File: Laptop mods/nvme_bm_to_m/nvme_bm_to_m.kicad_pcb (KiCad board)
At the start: 2 copper layers, 22 x 12.4 mm, 9 parts, among them J1 USB, U1 NGFF_M, U2 NGFF_B

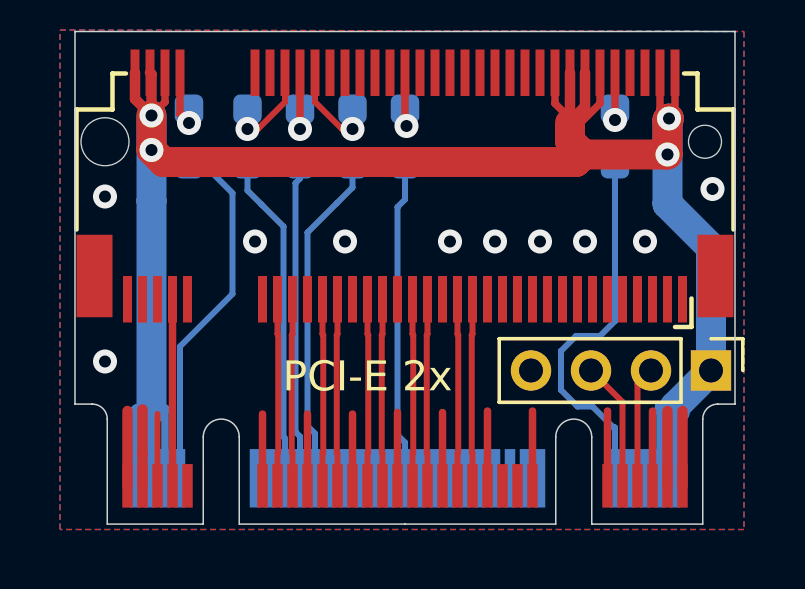
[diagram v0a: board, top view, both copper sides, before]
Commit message: Adding GND to the NVMe BM to M card shield
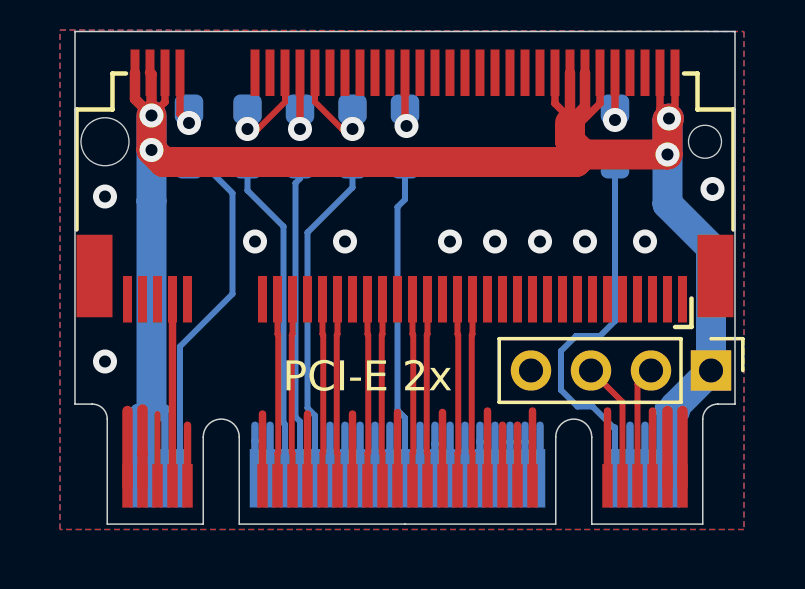
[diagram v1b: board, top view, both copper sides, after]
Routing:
- net Net-(U2-Pad67): track 0.00 -> 2.02 mm
- net Net-(U2-Pad25): track 0.00 -> 2.02 mm
- net Net-(U2-Pad23): track 0.00 -> 2.02 mm
- net Net-(U2-Pad8): track 0.00 -> 1.77 mm
- net Net-(U2-Pad6): track 0.00 -> 1.77 mm
- net Net-(U2-Pad58): track 0.00 -> 1.77 mm
- net Net-(U2-Pad56): track 0.00 -> 1.77 mm
- net Net-(U2-Pad48): track 0.00 -> 1.77 mm
- net Net-(U2-Pad46): track 0.00 -> 1.77 mm
- net Net-(U2-Pad44): track 0.00 -> 1.77 mm
- net Net-(U2-Pad42): track 0.00 -> 1.77 mm
- net Net-(U2-Pad40): track 0.00 -> 1.77 mm
- net Net-(U2-Pad36): track 0.00 -> 1.77 mm
- net Net-(U2-Pad34): track 0.00 -> 1.77 mm
- net Net-(U2-Pad32): track 0.00 -> 1.77 mm
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
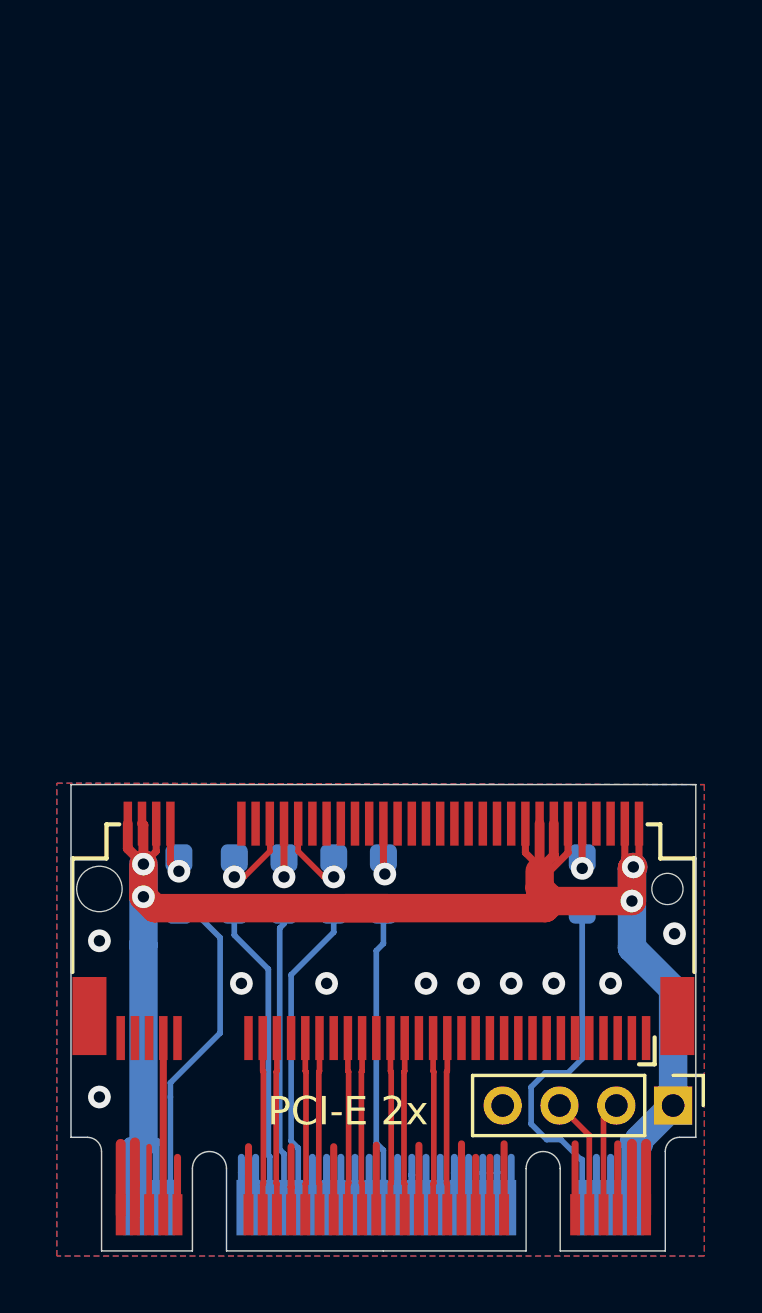
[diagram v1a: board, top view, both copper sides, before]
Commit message: Rerouted diffpairs to NVMe BM to M adapter, made the adapter longer, added holes so that part of the adapter can be snipped off for length decrease
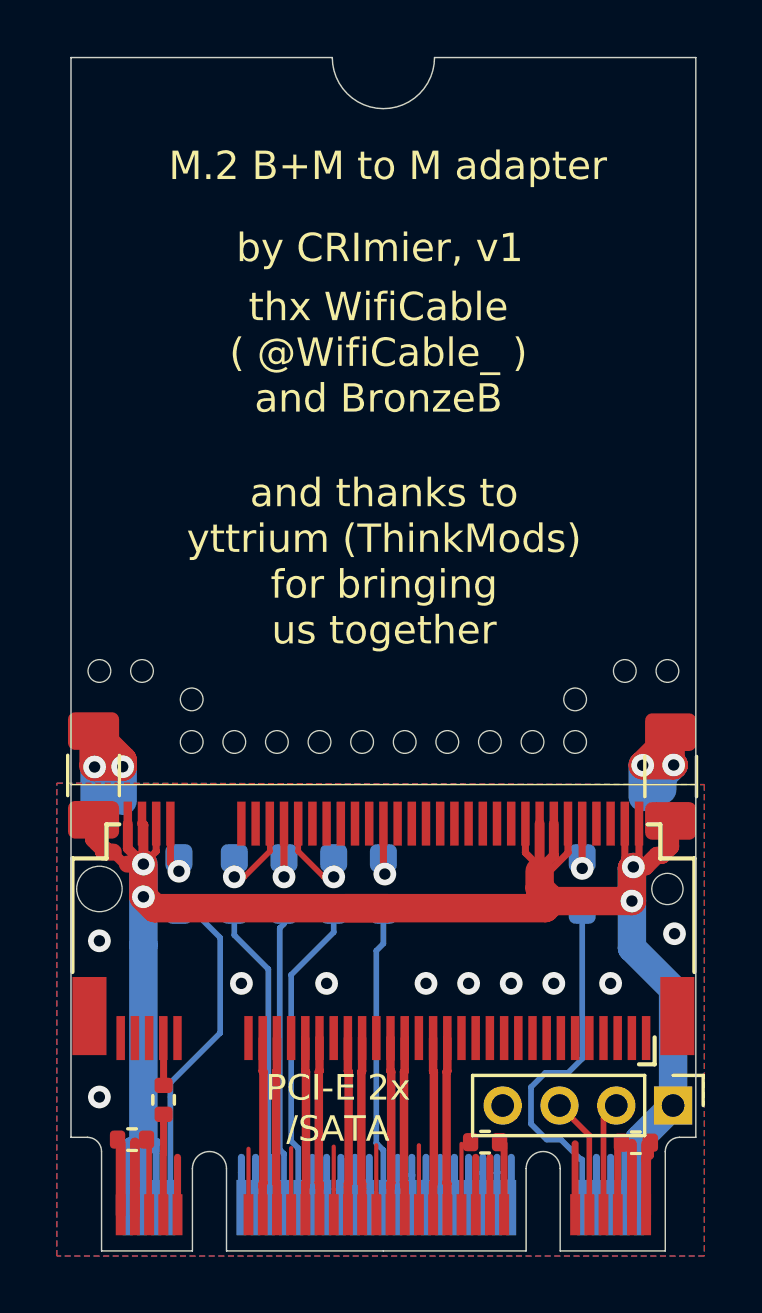
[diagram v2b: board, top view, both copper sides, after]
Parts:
- added C1: C_Small, Capacitor_SMD:C_1206_3216Metric_Pad1.33x1.80mm_HandSolder, F.Cu at (129.8, 154.2)
- added C2: C_Small, Capacitor_SMD:C_1206_3216Metric_Pad1.33x1.80mm_HandSolder, F.Cu at (150.1, 154.2)
- added R10: 0R, Resistor_SMD:R_0402_1005Metric, F.Cu at (131.2, 167.0)
- added R7: 0R, Resistor_SMD:R_0402_1005Metric, F.Cu at (148.9, 167.1)
- added R8: 0R, Resistor_SMD:R_0402_1005Metric, F.Cu at (143.6, 167.1)
- added R9: 0R, Resistor_SMD:R_0402_1005Metric, F.Cu at (132.3, 165.6)
- added REF**: hole, nvme_bm_to_m:hole, F.Cu at (146.8, 151.5)
- added REF**: hole, nvme_bm_to_m:hole, F.Cu at (137.8, 153.0)
- added REF**: hole, nvme_bm_to_m:hole, F.Cu at (136.2, 153.0)
- added REF**: hole, nvme_bm_to_m:hole, F.Cu at (134.8, 153.0)
- added REF**: hole, nvme_bm_to_m:hole, F.Cu at (130.0, 150.5)
- added REF**: hole, nvme_bm_to_m:hole, F.Cu at (131.5, 150.5)
- added REF**: hole, nvme_bm_to_m:hole, F.Cu at (133.2, 151.5)
- added REF**: hole, nvme_bm_to_m:hole, F.Cu at (133.2, 153.0)
- added REF**: hole, nvme_bm_to_m:hole, F.Cu at (148.5, 150.5)
- added REF**: hole, nvme_bm_to_m:hole, F.Cu at (150.0, 150.5)
- added REF**: hole, nvme_bm_to_m:hole, F.Cu at (146.8, 153.0)
- added REF**: hole, nvme_bm_to_m:hole, F.Cu at (145.2, 153.0)
- added REF**: hole, nvme_bm_to_m:hole, F.Cu at (143.8, 153.0)
- added REF**: hole, nvme_bm_to_m:hole, F.Cu at (142.2, 153.0)
- added REF**: hole, nvme_bm_to_m:hole, F.Cu at (140.8, 153.0)
- added REF**: hole, nvme_bm_to_m:hole, F.Cu at (139.2, 153.0)
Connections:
- U2 pad 1: GND -> Net-(R7-Pad1)
- U2 pad 21: GND -> Net-(R8-Pad1)
- U2 pad 69: /PCIE_~SATA -> Net-(R9-Pad1)
- U2 pad 75: GND -> Net-(R10-Pad1)
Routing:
- net +3V3: track 73.2 -> 82.0 mm
- net GND: track 34.5 -> 41.6 mm, vias 10 -> 14
- net /PCIE_~SATA: track 6.22 -> 1.67 mm
- net Net-(R9-Pad1): track 0.00 -> 3.54 mm
- net Net-(R7-Pad1): track 0.00 -> 3.16 mm
- net Net-(R8-Pad1): track 0.00 -> 2.50 mm
- net Net-(R10-Pad1): track 0.00 -> 2.50 mm
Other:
- board size 22 x 12.4 mm -> 22 x 38 mm
- rule trace_min: 0.2 -> 0.15
- board text added: "PCI-E 2x /SATA"
- board text added: "and thanks to yttrium (ThinkMods) for bringing us together"
- board text added: "thx WifiCable ( @WifiCable_ ) and BronzeB"
- board text removed: "PCI-E 2x"

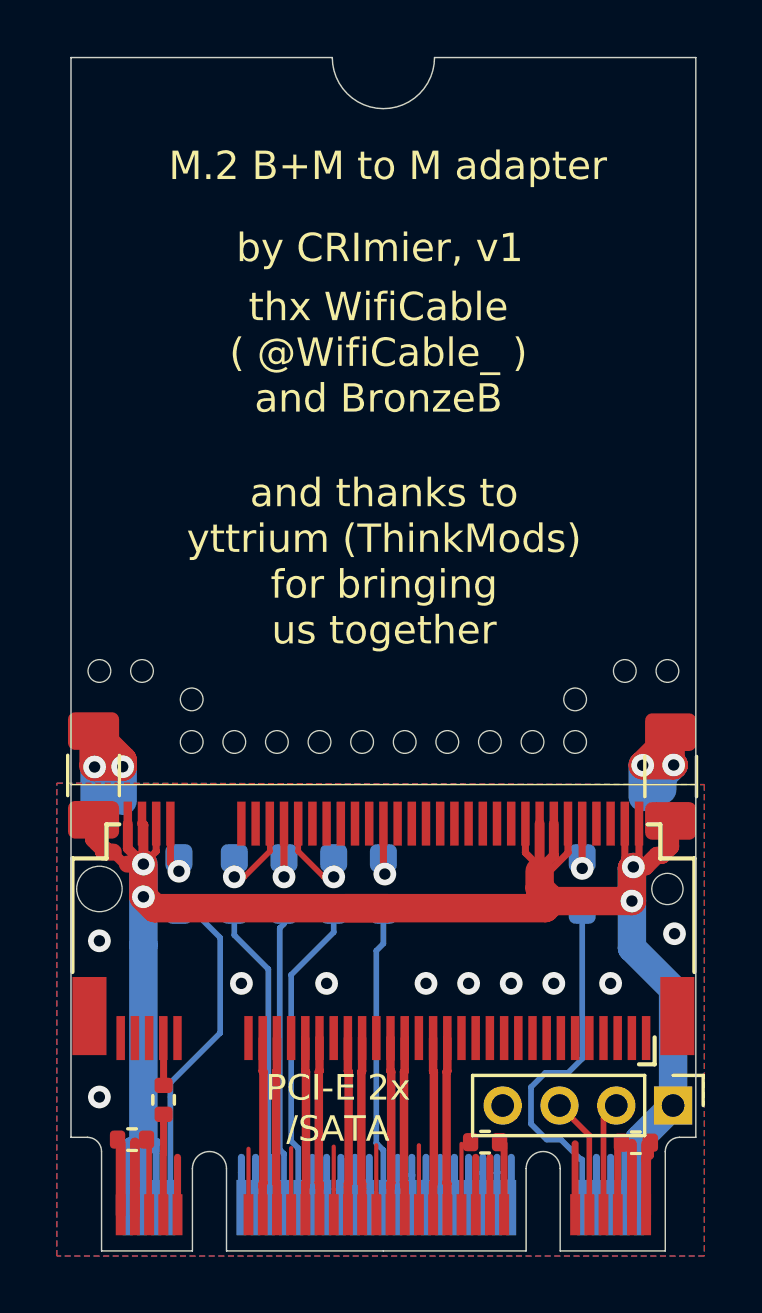
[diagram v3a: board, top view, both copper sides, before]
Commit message: nvme_bm_to_m: v2, removed caps, changed shape, isolated one ambiguous pin, updated README
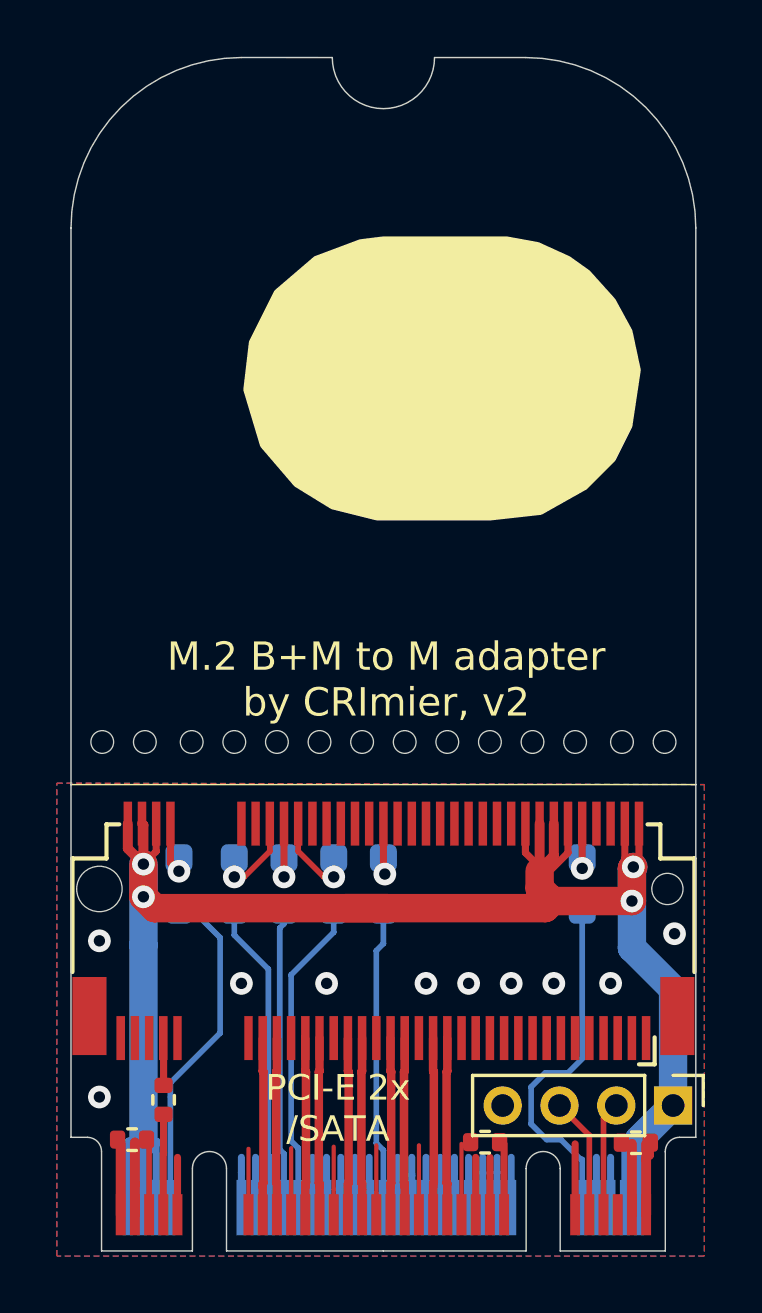
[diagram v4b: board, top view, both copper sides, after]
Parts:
- removed C1, C2: C_Small, Capacitor_SMD:C_1206_3216Metric_Pad1.33x1.80mm_HandSolder
- removed the REF** at (146.8, 151.5)
- removed the REF** at (133.2, 151.5)
- moved REF** 2.50 mm to (149.9, 153.0)
- moved REF** 2.50 mm to (148.4, 153.0)
- moved REF** 2.50 mm to (131.6, 153.0)
- moved REF** 2.50 mm to (130.1, 153.0)
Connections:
- net /PCIE_~SATA renamed /PCIE_~{SATA}
- net ~CLKREQ renamed ~{CLKREQ}
- net ~PERST renamed ~{PERST}
- net ~PEWAKE renamed ~{PEWAKE}
- U1 pad 11: Net-(U1-Pad11) -> unconnected-(U1-Pad11)
- U1 pad 13: Net-(U1-Pad13) -> unconnected-(U1-Pad13)
- U1 pad 17: Net-(U1-Pad17) -> unconnected-(U1-Pad17)
- U1 pad 19: Net-(U1-Pad19) -> unconnected-(U1-Pad19)
- U1 pad 20: Net-(U1-Pad20) -> unconnected-(U1-Pad20)
- U1 pad 22: Net-(U1-Pad22) -> unconnected-(U1-Pad22)
- U1 pad 23: Net-(U1-Pad23) -> unconnected-(U1-Pad23)
- U1 pad 24: Net-(U1-Pad24) -> unconnected-(U1-Pad24)
- U1 pad 25: Net-(U1-Pad25) -> unconnected-(U1-Pad25)
- U1 pad 26: Net-(U1-Pad26) -> unconnected-(U1-Pad26)
- U1 pad 28: Net-(U1-Pad28) -> unconnected-(U1-Pad28)
- U1 pad 30: Net-(U1-Pad30) -> unconnected-(U1-Pad30)
- U1 pad 32: Net-(U1-Pad32) -> unconnected-(U1-Pad32)
- U1 pad 34: Net-(U1-Pad34) -> unconnected-(U1-Pad34)
- U1 pad 36: Net-(U1-Pad36) -> unconnected-(U1-Pad36)
- U1 pad 40: Net-(U1-Pad40) -> unconnected-(U1-Pad40)
- U1 pad 42: Net-(U1-Pad42) -> unconnected-(U1-Pad42)
- U1 pad 44: Net-(U1-Pad44) -> unconnected-(U1-Pad44)
- U1 pad 46: Net-(U1-Pad46) -> unconnected-(U1-Pad46)
- U1 pad 48: Net-(U1-Pad48) -> unconnected-(U1-Pad48)
- U1 pad 5: Net-(U1-Pad5) -> unconnected-(U1-Pad5)
- U1 pad 56: Net-(U1-Pad56) -> unconnected-(U1-Pad56)
- U1 pad 58: Net-(U1-Pad58) -> unconnected-(U1-Pad58)
- U1 pad 6: Net-(U1-Pad6) -> unconnected-(U1-Pad6)
- U1 pad 67: Net-(U1-Pad67) -> unconnected-(U1-Pad67)
- U1 pad 7: Net-(U1-Pad7) -> unconnected-(U1-Pad7)
- U1 pad 8: Net-(U1-Pad8) -> unconnected-(U1-Pad8)
- U2 pad 20: Net-(U2-Pad20) -> unconnected-(U2-Pad20)
- U2 pad 22: Net-(U2-Pad22) -> unconnected-(U2-Pad22)
- U2 pad 23: Net-(U2-Pad23) -> unconnected-(U2-Pad23)
- U2 pad 24: Net-(U2-Pad24) -> unconnected-(U2-Pad24)
- U2 pad 25: Net-(U2-Pad25) -> unconnected-(U2-Pad25)
- U2 pad 26: Net-(U2-Pad26) -> unconnected-(U2-Pad26)
- U2 pad 28: Net-(U2-Pad28) -> unconnected-(U2-Pad28)
- U2 pad 30: Net-(U2-Pad30) -> unconnected-(U2-Pad30)
- U2 pad 32: Net-(U2-Pad32) -> unconnected-(U2-Pad32)
- U2 pad 34: Net-(U2-Pad34) -> unconnected-(U2-Pad34)
- U2 pad 36: Net-(U2-Pad36) -> unconnected-(U2-Pad36)
- U2 pad 40: Net-(U2-Pad40) -> unconnected-(U2-Pad40)
- U2 pad 42: Net-(U2-Pad42) -> unconnected-(U2-Pad42)
- U2 pad 44: Net-(U2-Pad44) -> unconnected-(U2-Pad44)
- U2 pad 46: Net-(U2-Pad46) -> unconnected-(U2-Pad46)
- U2 pad 48: Net-(U2-Pad48) -> unconnected-(U2-Pad48)
- U2 pad 5: GND -> unconnected-(U2-Pad5)
- U2 pad 56: Net-(U2-Pad56) -> unconnected-(U2-Pad56)
- U2 pad 58: Net-(U2-Pad58) -> unconnected-(U2-Pad58)
- U2 pad 6: Net-(U2-Pad6) -> unconnected-(U2-Pad6)
- U2 pad 67: Net-(U2-Pad67) -> unconnected-(U2-Pad67)
- U2 pad 8: Net-(U2-Pad8) -> unconnected-(U2-Pad8)
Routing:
- net GND: track 41.6 -> 24.4 mm, vias 14 -> 10
- net +3V3: track 82.0 -> 73.2 mm
- net unconnected-(U2-Pad67): track 0.00 -> 2.02 mm
- net unconnected-(U2-Pad25): track 0.00 -> 2.02 mm
- net unconnected-(U2-Pad23): track 0.00 -> 2.02 mm
- net Net-(U2-Pad67): track 2.02 -> 0.00 mm
- net Net-(U2-Pad25): track 2.02 -> 0.00 mm
- net Net-(U2-Pad23): track 2.02 -> 0.00 mm
- net unconnected-(U2-Pad8): track 0.00 -> 1.77 mm
- net unconnected-(U2-Pad6): track 0.00 -> 1.77 mm
- net unconnected-(U2-Pad58): track 0.00 -> 1.77 mm
- net unconnected-(U2-Pad56): track 0.00 -> 1.77 mm
- net unconnected-(U2-Pad48): track 0.00 -> 1.77 mm
- net unconnected-(U2-Pad46): track 0.00 -> 1.77 mm
- net unconnected-(U2-Pad44): track 0.00 -> 1.77 mm
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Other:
- outline, holes or cut-outs redrawn
- net class Default removed
- board text added: "M.2 B+M to M adapter by CRImier, v2"
- board text added: "M.2 B+M to M adapter by CRImier, v2 thx WifiCable ( @WifiCable_ ) and BronzeB and thanks to yttrium (ThinkMods) for bringing us together"
- board text added: "by CRImier, v2"
- board text added: "trans rights"
- board text removed: "and thanks to yttrium (ThinkMods) for bringing us together"
- board text removed: "by CRImier, v1"
- board text removed: "thx WifiCable ( @WifiCable_ ) and BronzeB"
